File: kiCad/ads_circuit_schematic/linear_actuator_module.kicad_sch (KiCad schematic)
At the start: 0 parts

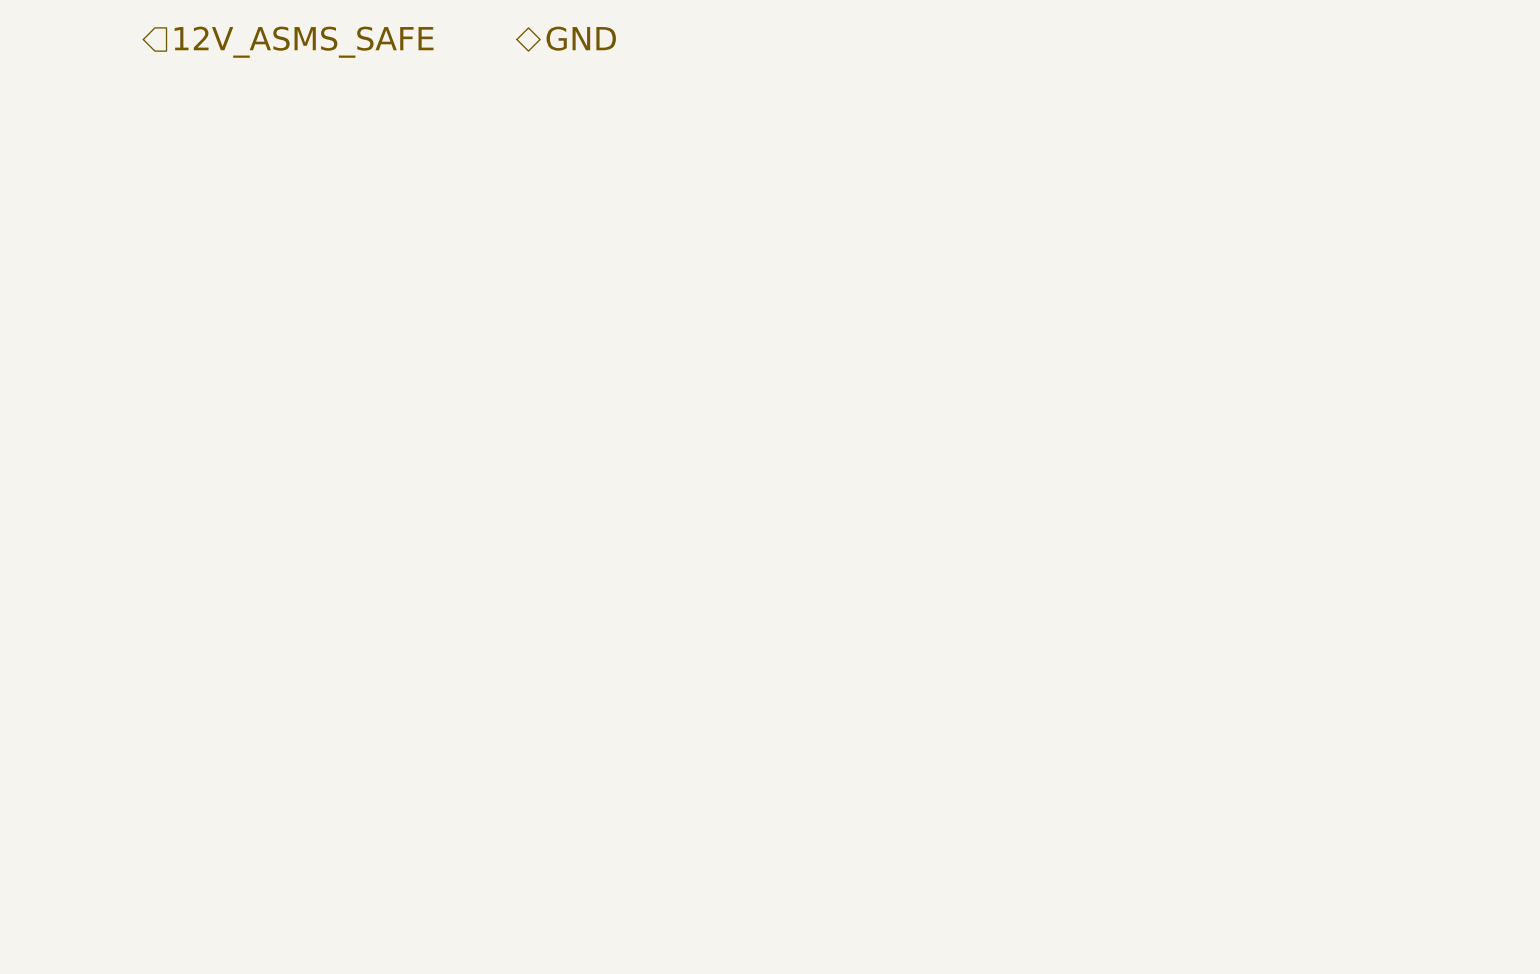
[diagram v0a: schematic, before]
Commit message: Added new symbols for linear actuators, added fuses, added 5V step down
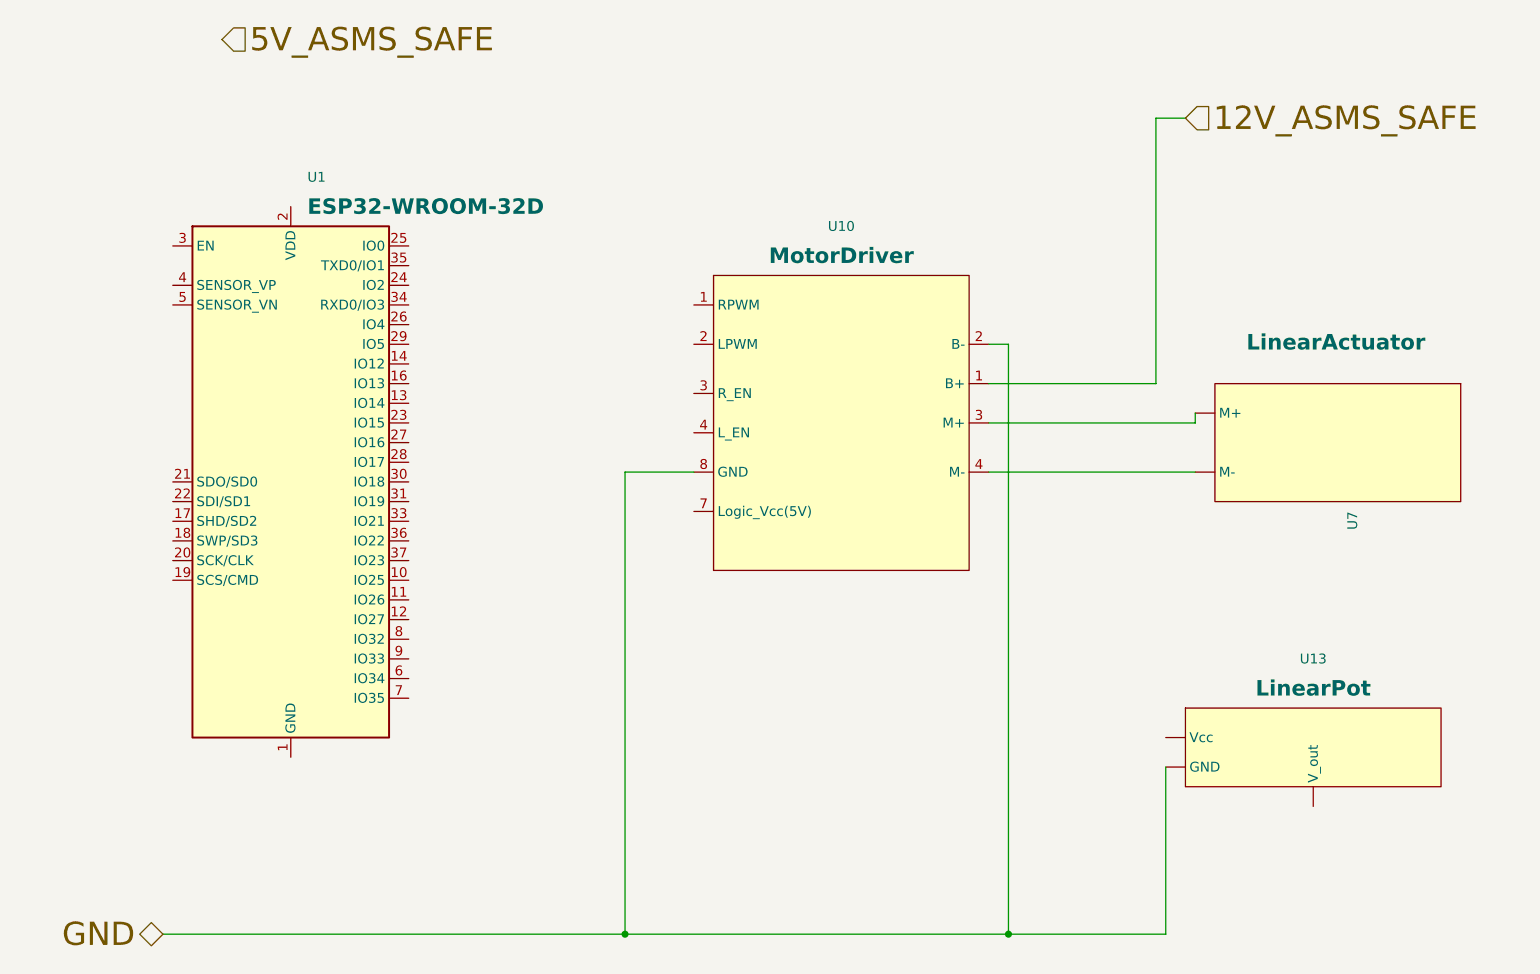
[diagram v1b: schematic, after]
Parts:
- added U1: ESP32-WROOM-32D, RF_Module:ESP32-WROOM-32D, symbol RF_Module:ESP32-WROOM-32D
- added U10: MotorDriver, symbol LinearActuatorModuleLibrary:MotorDriver
- added U13: LinearPot, symbol LinearActuatorModuleLibrary:LinearPot
- added U7: LinearActuator, symbol LinearActuatorModuleLibrary:LinearActuator
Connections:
- net 12V_ASMS_SAFE: now also U10.1 (B+)
- net GND: now also U10.2 (B-), U10.8 (GND), U13. (V_out)
- new net: U10.3 (M+), U7. (M-)
- new net: U10.4 (M-), U7. (M-)
- new net: U1.1 (GND), U1.15 (GND), U1.38 (GND), U1.39 (GND)

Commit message: finished linear actuator wiring diagram
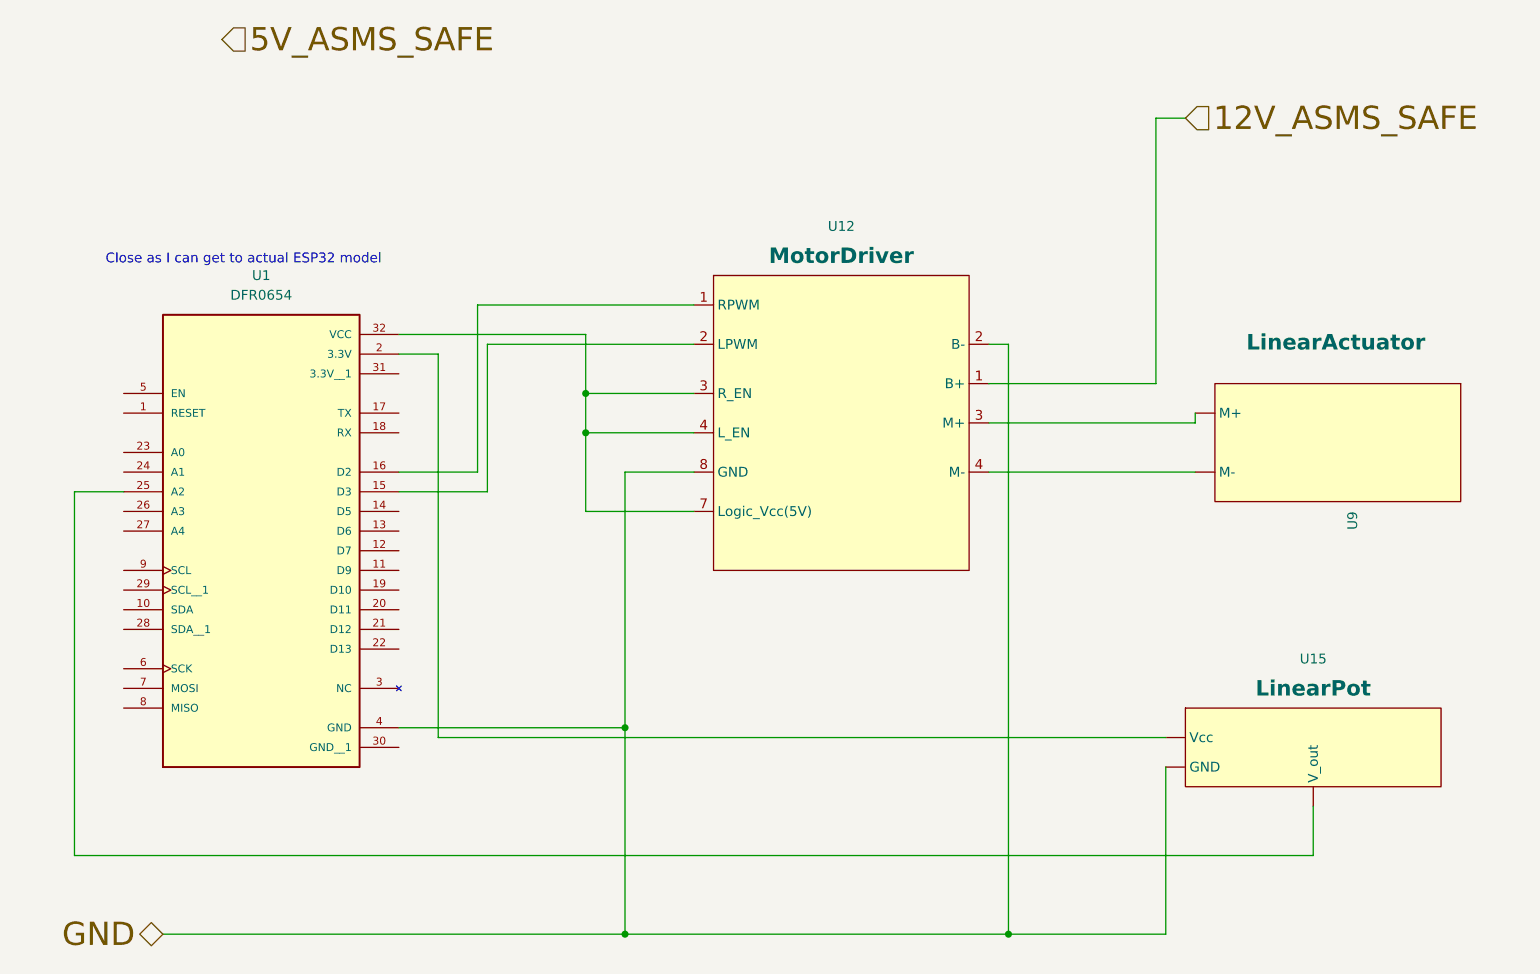
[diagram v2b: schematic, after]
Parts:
- removed U1: ESP32-WROOM-32D, RF_Module:ESP32-WROOM-32D, symbol RF_Module:ESP32-WROOM-32D
- added U1: DFR0654, DFR0654:MODULE_DFR0654, symbol DFR0654:DFR0654
- renumbered U10 to U12, U13 to U15, U7 to U9
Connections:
- net GND: now also U1.4 (GND)
- net at U9. (M-): now also U12.4 (M-); no longer U12.3 (M+)
- net at U12.4 (M-): now also U12.3 (M+), U12.7 (Logic_Vcc(5V)), U1.32 (VCC); no longer U9. (M-)
- new net: U12.3 (M+), U9. (M-)
- new net: U1.2 (3.3V), U15. (V_out)
- new net: U1.25 (A2), U15. (V_out)
- new net: U1.16 (D2), U12.1 (B+)
- new net: U1.15 (D3), U12.2 (B-)
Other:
- note added: "Close as I can get to actual ESP32 model"

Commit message: added breaking motor
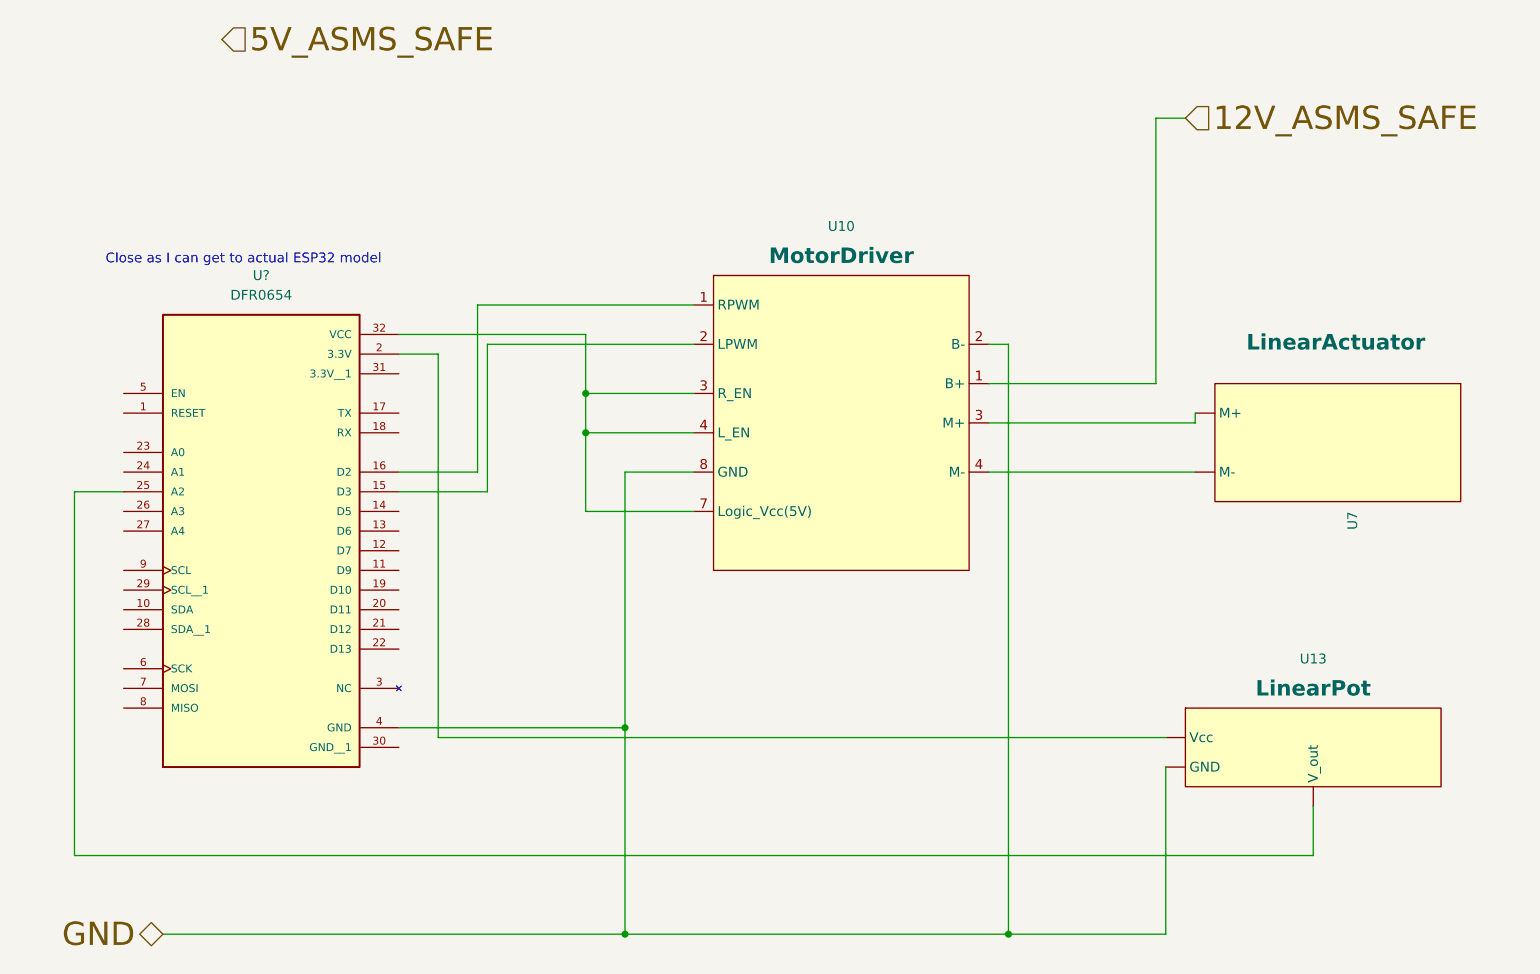
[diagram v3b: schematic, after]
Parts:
- renumbered U12 to U10, U15 to U13, U9 to U7, U1 to U?
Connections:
- net at U7. (M-): now also U10.4 (M-); no longer U10.3 (M+)
- net at U10.4 (M-): now also U10.3 (M+), U10.7 (Logic_Vcc(5V)), U?.32 (VCC); no longer U7. (M-)
- new net: U10.3 (M+), U7. (M-)
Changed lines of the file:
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@@
 		(on_board yes)
 		(dnp no)
-		(property "Reference" "U?"
+		(property "Reference" "U7"
 			(at 187.9601 88.9 0)
 			(effects
@@
 		(dnp no)
 		(fields_autoplaced yes)
-		(property "Reference" "U?"
+		(property "Reference" "U13"
 			(at 182.88 107.95 0)
 			(effects
@@
 		(dnp no)
 		(fields_autoplaced yes)
-		(property "Reference" "U?"
+		(property "Reference" "U10"
 			(at 121.92 52.07 0)
 			(effects
@@
 		(dnp no)
 		(fields_autoplaced yes)
-		(property "Reference" "U1"
+		(property "Reference" "U?"
 			(at 46.99 58.42 0)
 			(effects
@@
 		)
 		(instances
+			(project "ads_circuit_schematic"
+				(path "/71fa6abf-14fe-4383-b55d-b9c0203d051b/6ebb9076-ee1d-476e-8ec6-663f05d44008"
+					(reference "U?")
+					(unit 1)
+				)
+				(path "/71fa6abf-14fe-4383-b55d-b9c0203d051b/d3b3d7c6-59fe-4ce9-9e2a-b0d36ac8ff03"
+					(reference "U?")
+					(unit 1)
+				)
+				(path "/71fa6abf-14fe-4383-b55d-b9c0203d051b/f891a5f4-e8a4-494d-93e7-aeaac863b432"
+					(reference "U?")
+					(unit 1)
+				)
+			)
 			(project ""
 				(path "/c85e4fec-a7c3-4bb6-ab70-7c34bdc77984"

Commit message: updated actuator schematic
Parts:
- added U2: TXB0104D, Package_SO:SOIC-14_3.9x8.7mm_P1.27mm, symbol Logic_LevelTranslator:TXB0104D
- gave numbers to parts that had none: 1
- renumbered U10 to U12, U13 to U15, U7 to U9
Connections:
- net GND: now also U2.7 (GND)
- net at U9. (M-): now also U12.4 (M-); no longer U12.3 (M+)
- net at U12.4 (M-): now also U2.10 (B4); no longer U9. (M-)
- net at U1.2 (3.3V), U15. (V_out): now also U2.1 (VCCA)
- net at U1.16 (D2): no longer U12.1 (B+)
- net at U1.15 (D3): no longer U12.2 (B-)
- net at U1.32 (VCC), U12.7 (Logic_Vcc(5V)): now also U2.14 (VCCB); no longer U12.3 (M+), U12.4 (M-)
- net at U1.11 (D9): now also U2.4 (A3)
- net at U1.12 (D7): now also U2.2 (A1)
- net at U1.13 (D6): now also U2.8 (OE)
- net at U1.19 (D10): now also U2.5 (A4)
- new net: U12.3 (M+), U9. (M-)
- new net: U12.1 (B+), U2.13 (B1)
- new net: U12.2 (B-), U2.12 (B2)
- new net: U12.3 (M+), U2.11 (B3)
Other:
- note added: "not the actual model, but represents function"
- moved on the sheet: U1, U15
